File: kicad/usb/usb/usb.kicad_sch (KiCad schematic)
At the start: 20 parts, among them J1 USB_C_Receptacle_USB2.0_14P, J2 PH2.0mm 2P, J3 Conn_01x07_Pin, Q1 MMBT3906, SW1 PWR, U1 S-T111B33MC-OGSTFU, U2 MCP73831-2-OT

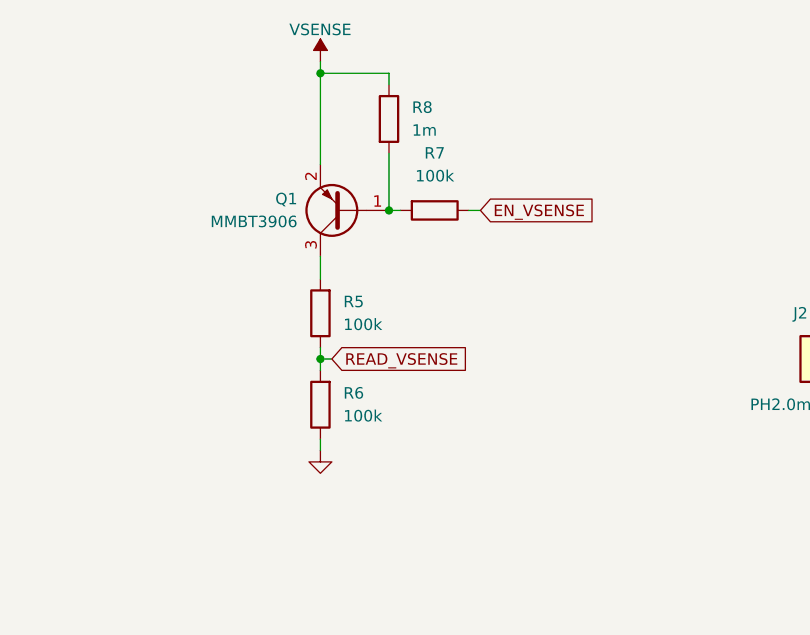
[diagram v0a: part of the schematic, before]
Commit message: Getting rid of the vdiv switch after some testing
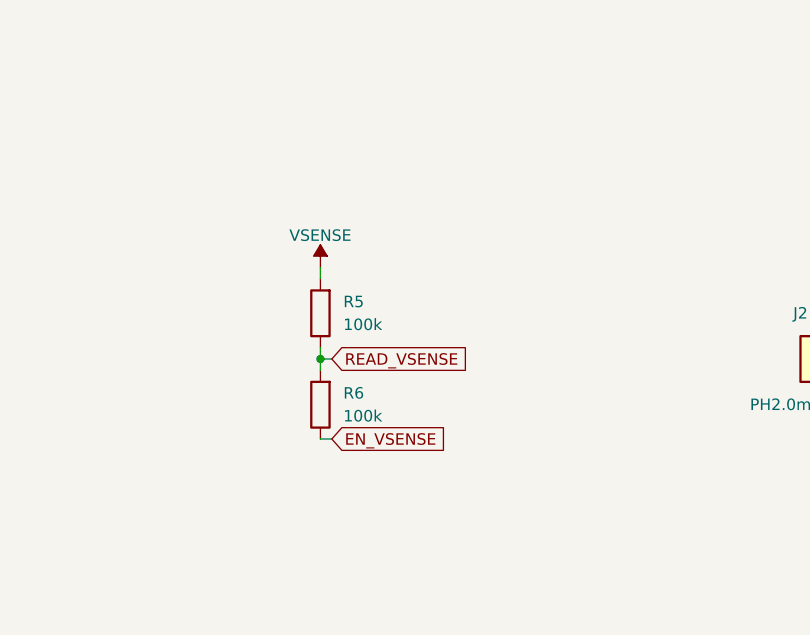
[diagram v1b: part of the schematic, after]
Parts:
- removed Q1: MMBT3906, Package_TO_SOT_SMD:SOT-23, symbol Transistor_BJT:MMBT3906
- removed R7: 100k, Resistor_SMD:R_0402_1005Metric_Pad0.72x0.64mm_HandSolder, symbol Device:R
- removed R8: 1m, Resistor_SMD:R_0402_1005Metric_Pad0.72x0.64mm_HandSolder, symbol Device:R
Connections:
- net EN_VSENSE: now also R6.1
- net GND: no longer R6.1
- net VSENSE: now also R5.2
